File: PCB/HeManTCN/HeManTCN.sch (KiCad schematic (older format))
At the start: 109 parts, among them J101 VBATG, J102 VBAT+, J103 Micro_SD_Card, J104 Conn_02x03_Odd_Even, J105 Conn_02x02_Odd_Even, J106 Conn_02x05_Odd_Even, J107 Conn_02x12_Odd_Even, J108 Conn_02x12_Odd_Even, J109 Conn_02x05_Odd_Even, J110 Conn_02x12_Odd_Even, J111 USB_B, J112 USB_B, J113 73725-0110BLF, J114 Screw_Terminal_01x06, J115 RJ45_Amphenol_RJMG1BD3B8K1ANR, J116 Screw_Terminal_01x02, SW101 RESET, SW102 PC13, U101 STM32H743VITx, U102 MVBC02D, U103 S25FL127SABMFI101, U104 STM32F042F6Px, U105 TCAN332, U106 ISL83483, U107 USBLC6-2SC6, U108 KSZ8081RNA, U109 USBLC6-2SC6, U110 USBLC6-2SC6, U111 MIC2005A, U112 AP63203, Y101 8MHz, Y102 32.768KHz, Y103 25MHz

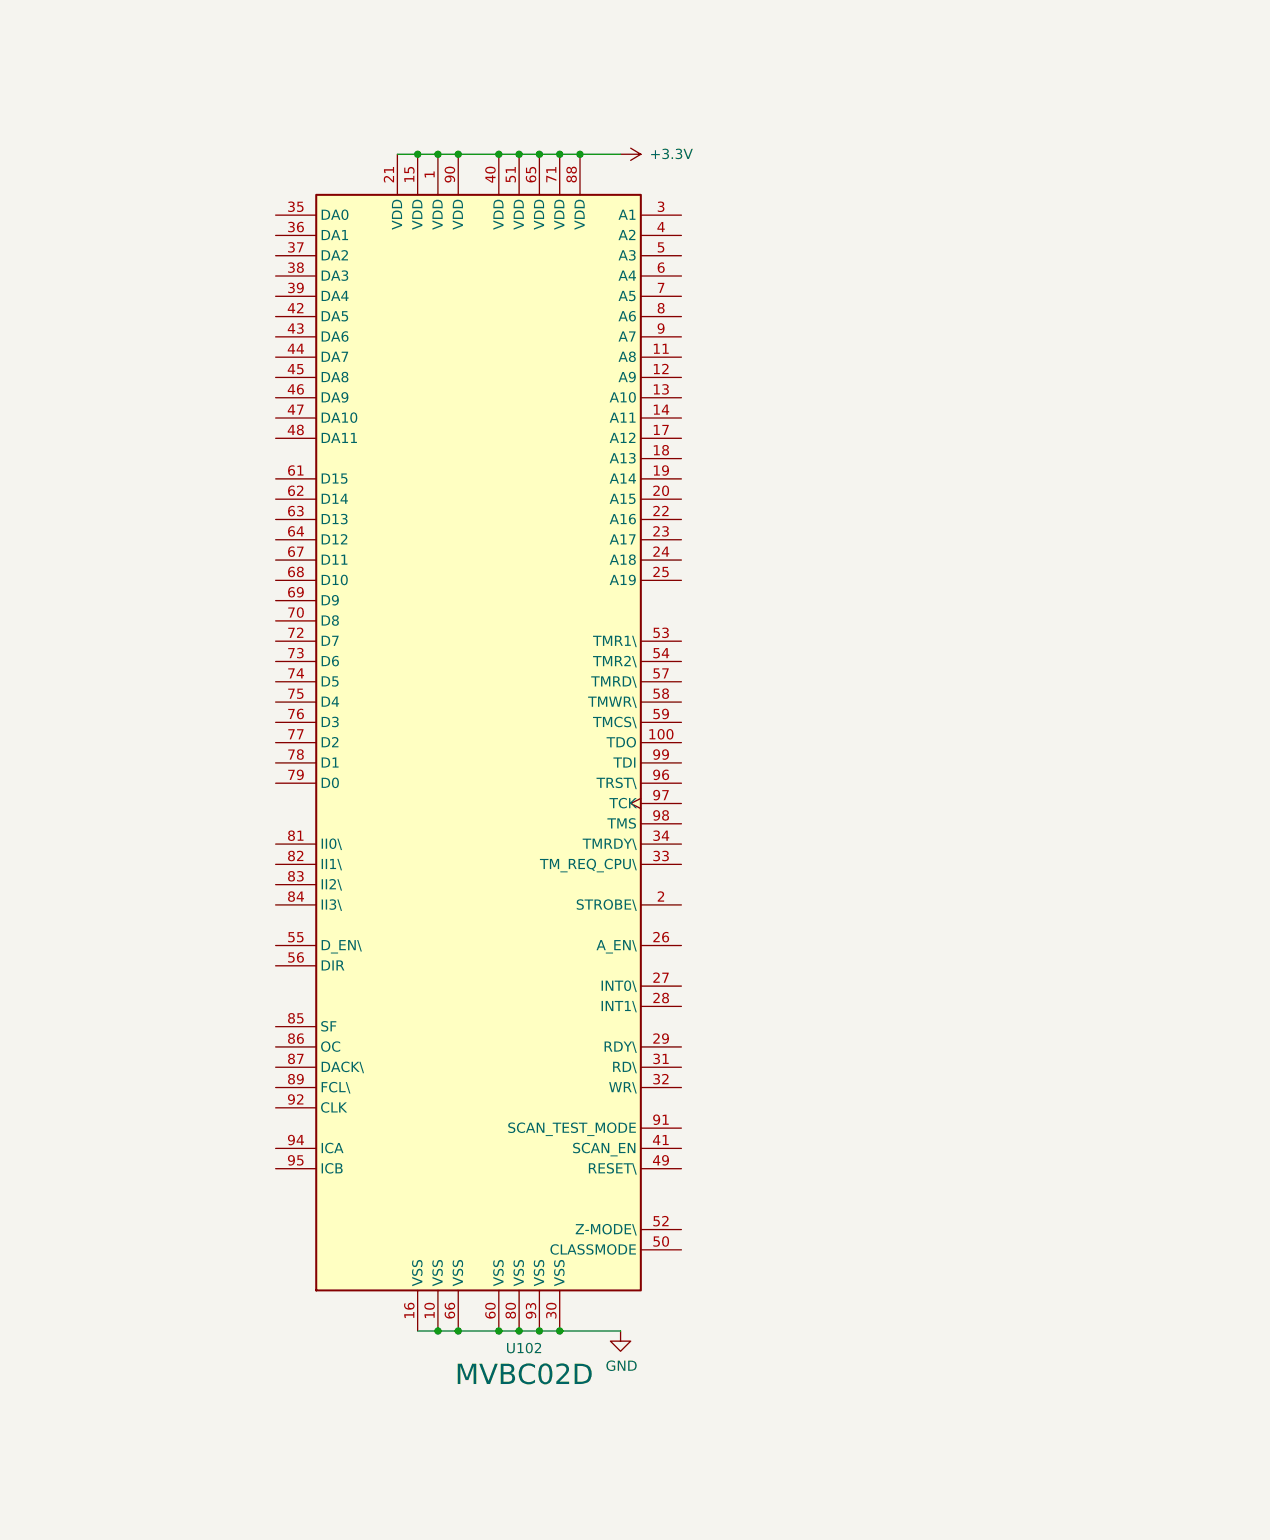
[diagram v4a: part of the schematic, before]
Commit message: Esquematico con Memoria
Ahora esta la memoria en el esquematico. Faltan las conecciones.
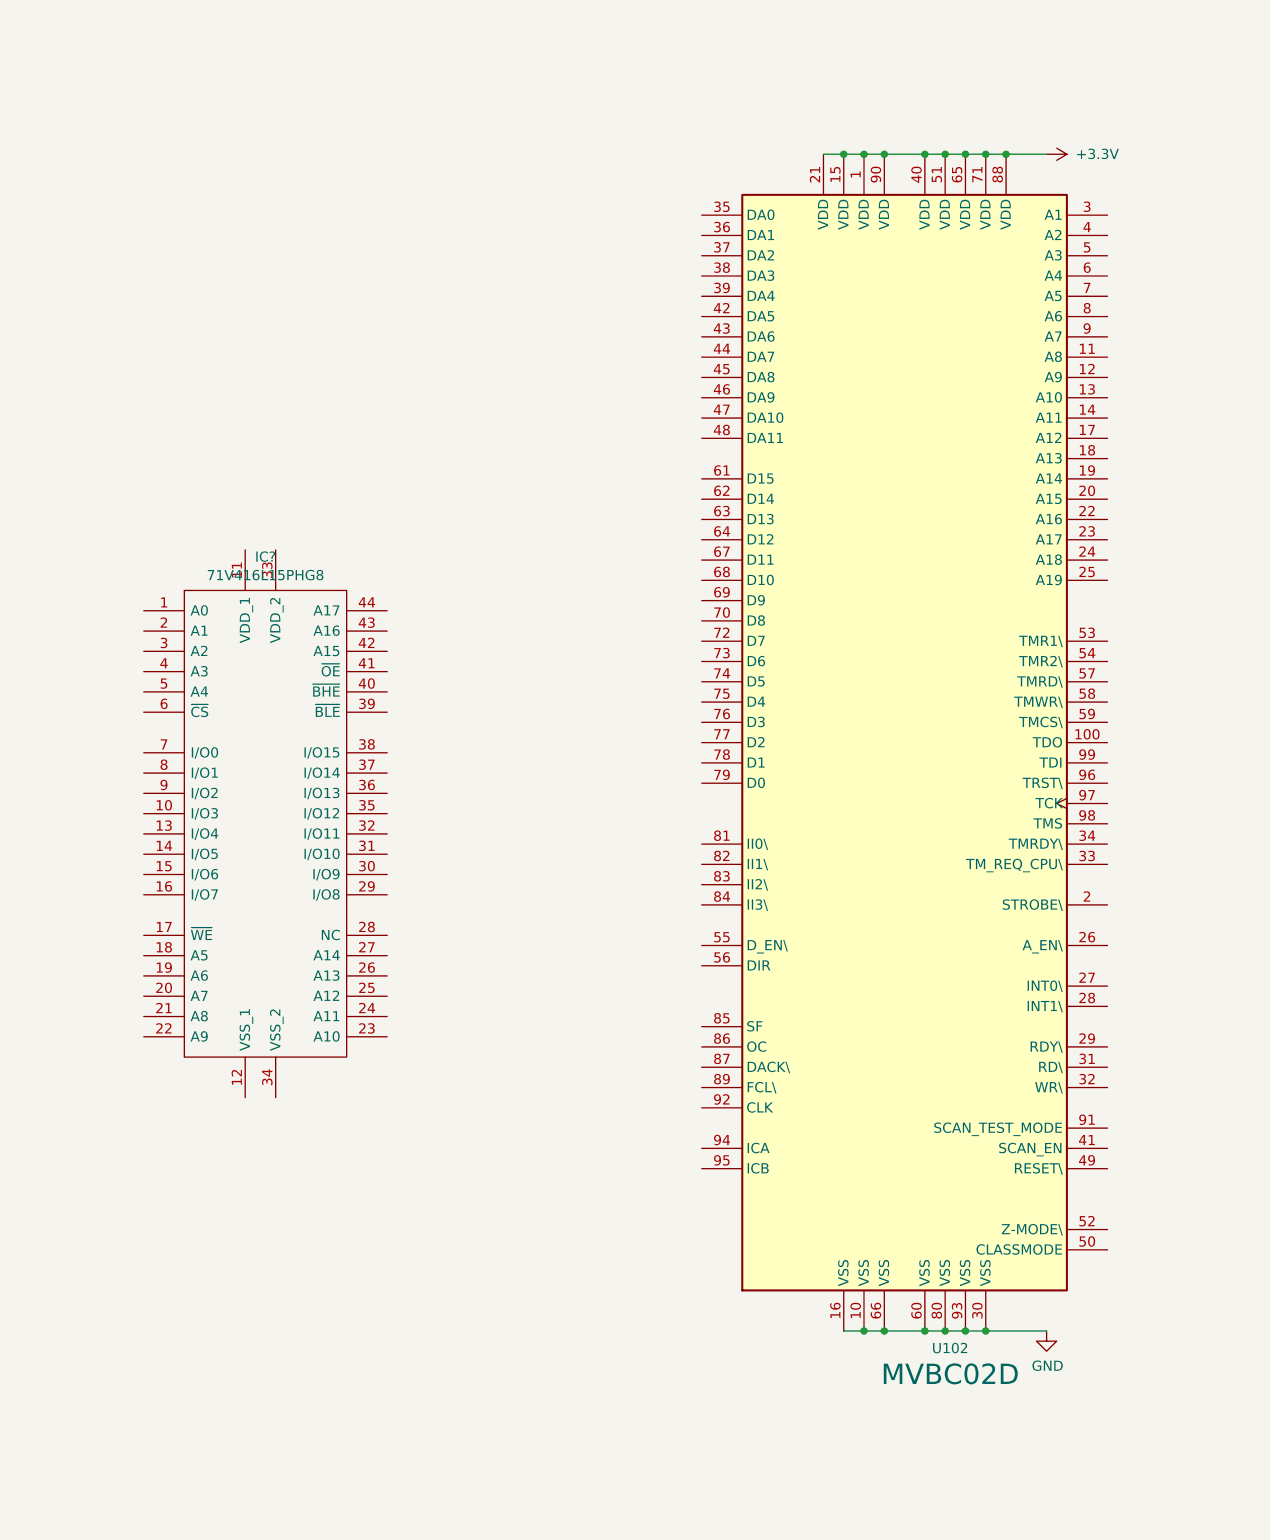
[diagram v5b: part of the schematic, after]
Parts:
- added IC?: 71V416L15PHG8, SOP80P1176X120-44N, symbol 71V416L15PHG8:71V416L15PHG8
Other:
- moved on the sheet: U102
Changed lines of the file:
@@
 L Bombardier:MVBC02D U?
 U 1 1 5DA67866
-P 8100 5150
+P 10200 5150
 AR Path="/5D9FB101/5DA67866" Ref="U?"  Part="1"
 AR Path="/5DA67866" Ref="U102"  Part="1"
-F 0 "U102" H 8325 2164 50  0000 C CNN
-F 1 "MVBC02D" H 8325 2035 100 0000 C CNN
-F 2 "Package_QFP:QFP-100_14x20mm_P0.5mm" H 7300 2450 50  0001 R CNN
-F 3 "TEXTO" H 7400 8050 50  0001 C CNN
-	1    8100 5150
+F 0 "U102" H 10425 2164 50  0000 C CNN
+F 1 "MVBC02D" H 10425 2035 100 0000 C CNN
+F 2 "Package_QFP:QFP-100_14x20mm_P0.5mm" H 9400 2450 50  0001 R CNN
+F 3 "TEXTO" H 9500 8050 50  0001 C CNN
+	1    10200 5150
 	1    0    0    -1
 $EndComp
@@
 L power:+3.3V #PWR0185
 U 1 1 5DADCB1A
-P 8800 2250
+P 10900 2250
 AR Path="/5DADCB1A" Ref="#PWR0185"  Part="1"
 AR Path="/5DA2C15A/5DADCB1A" Ref="#PWR?"  Part="1"
-F 0 "#PWR0185" H 8800 2100 50  0001 C CNN
-F 1 "+3.3V" V 8800 2500 50  0000 C CNN
-F 2 "" H 8800 2250 50  0001 C CNN
-F 3 "" H 8800 2250 50  0001 C CNN
-	1    8800 2250
+F 0 "#PWR0185" H 10900 2100 50  0001 C CNN
+F 1 "+3.3V" V 10900 2500 50  0000 C CNN
+F 2 "" H 10900 2250 50  0001 C CNN
+F 3 "" H 10900 2250 50  0001 C CNN
+	1    10900 2250
 	0    1    1    0
 $EndComp
 Wire Wire Line
-	8800 2250 8600 2250
-Wire Wire Line
-	8500 2250 8400 2250
-Wire Wire Line
-	8600 2250 8500 2250
-Connection ~ 8600 2250
-Connection ~ 8500 2250
-Wire Wire Line
-	8400 2250 8300 2250
-Connection ~ 8400 2250
-Wire Wire Line
-	8300 2250 8200 2250
-Connection ~ 8300 2250
-Wire Wire Line
-	8200 2250 8000 2250
-Connection ~ 8200 2250
-Wire Wire Line
-	8000 2250 7900 2250
-Connection ~ 8000 2250
-Wire Wire Line
-	7900 2250 7800 2250
-Connection ~ 7900 2250
-Wire Wire Line
-	7800 2250 7700 2250
-Connection ~ 7800 2250
+	10900 2250 10700 2250
+Wire Wire Line
+	10600 2250 10500 2250
+Wire Wire Line
+	10700 2250 10600 2250
+Connection ~ 10700 2250
+Connection ~ 10600 2250
+Wire Wire Line
+	10500 2250 10400 2250
+Connection ~ 10500 2250
+Wire Wire Line
+	10400 2250 10300 2250
+Connection ~ 10400 2250
+Wire Wire Line
+	10300 2250 10100 2250
+Connection ~ 10300 2250
+Wire Wire Line
+	10100 2250 10000 2250
+Connection ~ 10100 2250
+Wire Wire Line
+	10000 2250 9900 2250
+Connection ~ 10000 2250
+Wire Wire Line
+	9900 2250 9800 2250
+Connection ~ 9900 2250
 $Comp
 L power:GND #PWR0186
 U 1 1 5DB5E868
-P 8800 8050
+P 10900 8050
 AR Path="/5DB5E868" Ref="#PWR0186"  Part="1"
 AR Path="/5DA2C15A/5DB5E868" Ref="#PWR?"  Part="1"
-F 0 "#PWR0186" H 8800 7800 50  0001 C CNN
-F 1 "GND" H 8805 7877 50  0000 C CNN
-F 2 "" H 8800 8050 50  0001 C CNN
-F 3 "" H 8800 8050 50  0001 C CNN
-	1    8800 8050
-	1    0    0    -1
-$EndComp
-Wire Wire Line
-	8800 8050 8500 8050
-Wire Wire Line
-	8500 8050 8400 8050
-Connection ~ 8500 8050
-Wire Wire Line
-	8400 8050 8300 8050
-Connection ~ 8400 8050
-Wire Wire Line
-	8300 8050 8200 8050
-Connection ~ 8300 8050
-Wire Wire Line
-	8200 8050 8000 8050
-Connection ~ 8200 8050
-Wire Wire Line
-	7900 8050 8000 8050
-Connection ~ 8000 8050
-Wire Wire Line
-	7900 8050 7800 8050
-Connection ~ 7900 8050
+F 0 "#PWR0186" H 10900 7800 50  0001 C CNN
+F 1 "GND" H 10905 7877 50  0000 C CNN
+F 2 "" H 10900 8050 50  0001 C CNN
+F 3 "" H 10900 8050 50  0001 C CNN
+	1    10900 8050
+	1    0    0    -1
+$EndComp
+Wire Wire Line
+	10900 8050 10600 8050
+Wire Wire Line
+	10600 8050 10500 8050
+Connection ~ 10600 8050
+Wire Wire Line
+	10500 8050 10400 8050
+Connection ~ 10500 8050
+Wire Wire Line
+	10400 8050 10300 8050
+Connection ~ 10400 8050
+Wire Wire Line
+	10300 8050 10100 8050
+Connection ~ 10300 8050
+Wire Wire Line
+	10000 8050 10100 8050
+Connection ~ 10100 8050
+Wire Wire Line
+	10000 8050 9900 8050
+Connection ~ 10000 8050
+$Comp
+L 71V416L15PHG8:71V416L15PHG8 IC?
+U 1 1 5DA88F9D
+P 6450 4500
+F 0 "IC?" H 7050 4765 50  0000 C CNN
+F 1 "71V416L15PHG8" H 7050 4674 50  0000 C CNN
+F 2 "SOP80P1176X120-44N" H 7500 4600 50  0001 L CNN
+F 3 "https://componentsearchengine.com/Datasheets/1/71V416L15PHG8.pdf" H 7500 4500 50  0001 L CNN
+F 4 "SRAM 256Kx16 ASYNCHRONOUS 3.3V CMOS SRAM" H 7500 4400 50  0001 L CNN "Description"
+F 5 "1.2" H 7500 4300 50  0001 L CNN "Height"
+F 6 "972-71V416L15PHG8" H 7500 4200 50  0001 L CNN "Mouser Part Number"
+F 7 "https://www.mouser.com/Search/Refine.aspx?Keyword=972-71V416L15PHG8" H 7500 4100 50  0001 L CNN "Mouser Price/Stock"
+F 8 "IDT" H 7500 4000 50  0001 L CNN "Manufacturer_Name"
+F 9 "71V416L15PHG8" H 7500 3900 50  0001 L CNN "Manufacturer_Part_Number"
+	1    6450 4500
+	1    0    0    -1
+$EndComp
 $EndSCHEMATC
